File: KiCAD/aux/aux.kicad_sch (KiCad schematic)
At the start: 5 parts, among them J1 PMOD_male_2row, J2 Conn_01x12_Socket

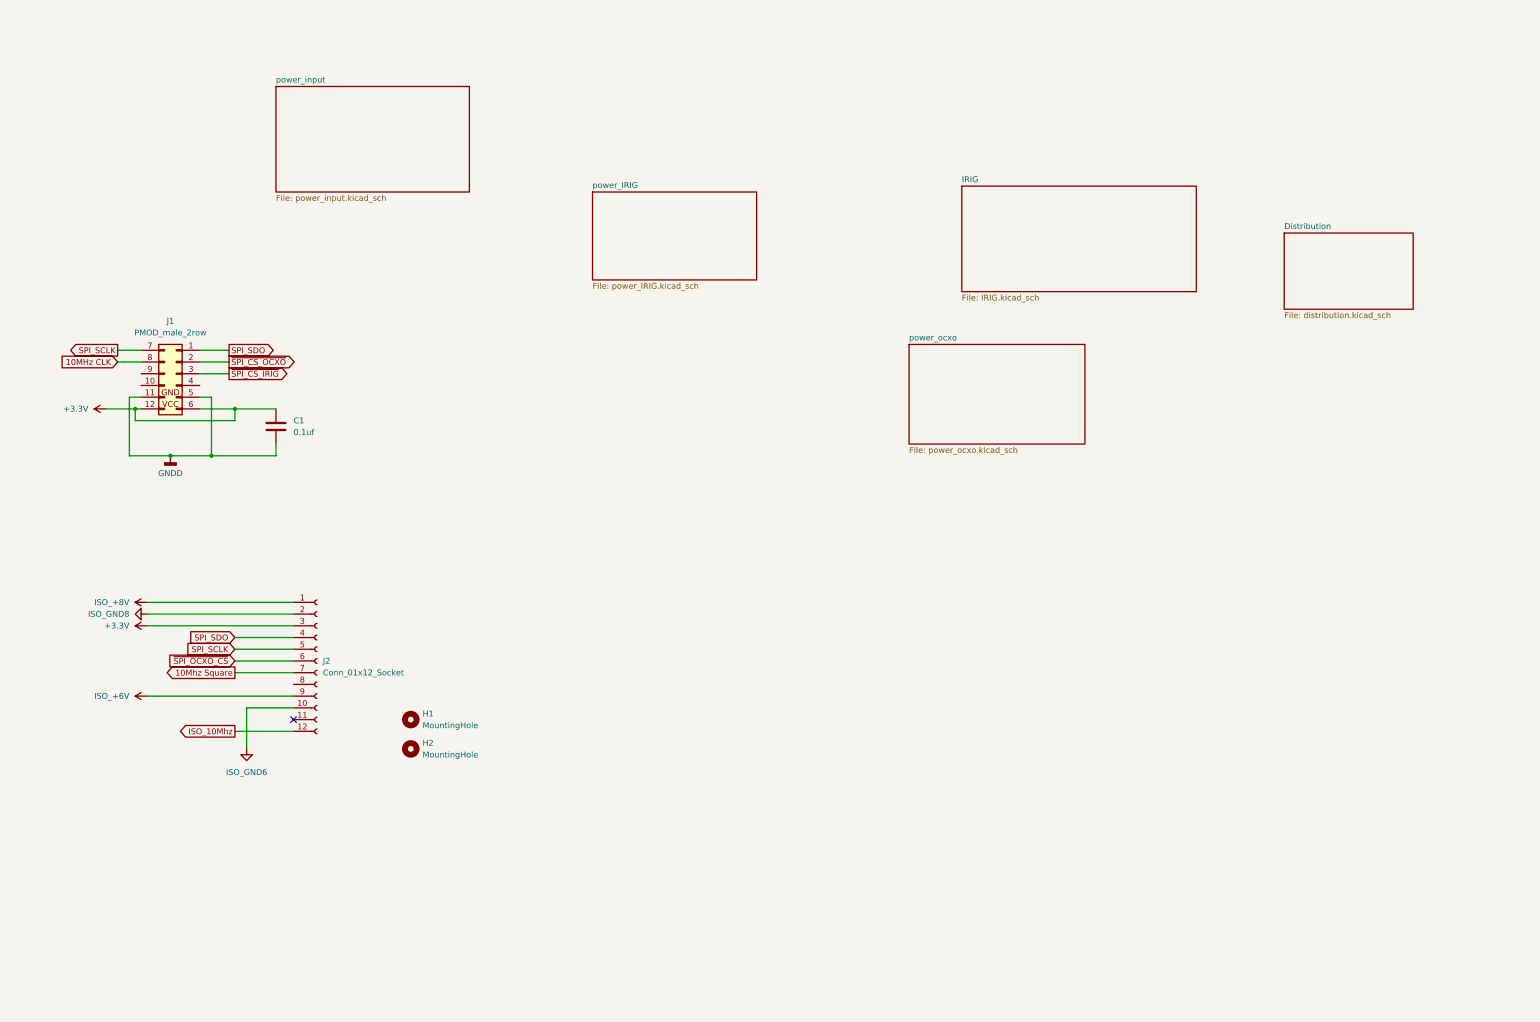
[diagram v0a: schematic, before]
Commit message: Reworked, now with IRIG option board complete
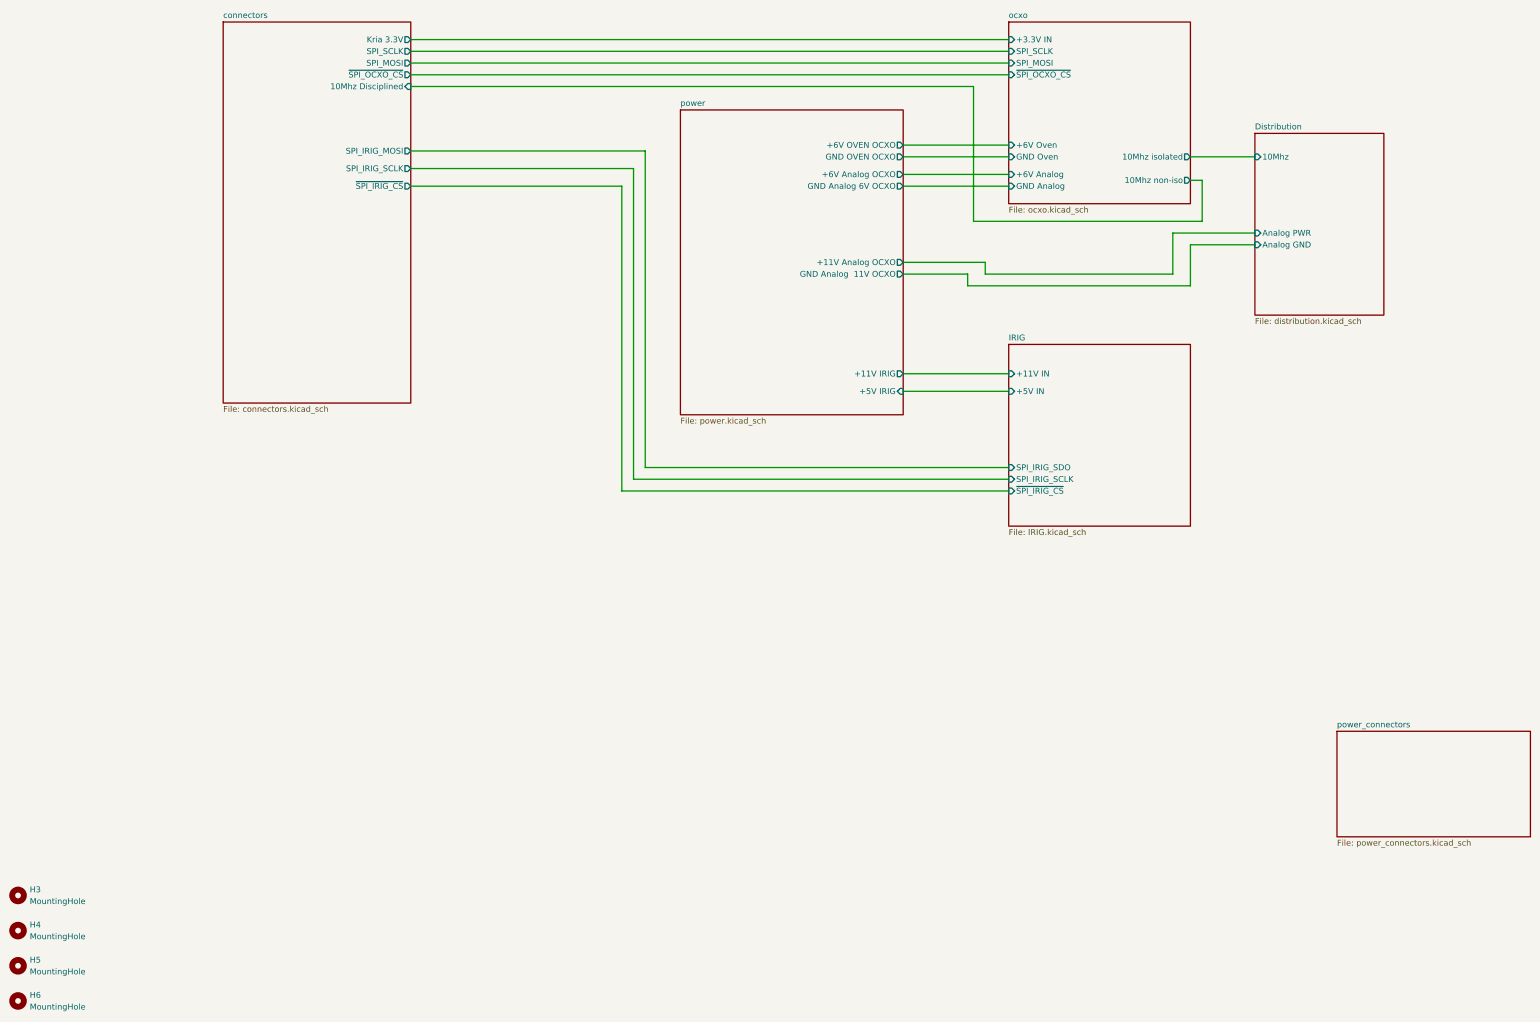
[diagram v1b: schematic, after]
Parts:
- removed C1: 0.1uf, Capacitor_SMD:C_1206_3216Metric_Pad1.33x1.80mm_HandSolder, symbol Device:C
- removed H1, H2: MountingHole, MountingHole:MountingHole_3.2mm_M3, symbol Mechanical:MountingHole
- removed J1: PMOD_male_2row, ! Scott:PMOD_male_12pin, symbol ! Scott:PMOD_male_2row
- removed J2: Conn_01x12_Socket, Connector_PinSocket_2.54mm:PinSocket_1x12_P2.54mm_Vertical, symbol Connector:Conn_01x12_Socket
- added H3, H4, H5, H6: MountingHole, MountingHole:MountingHole_3.2mm_M3, symbol Mechanical:MountingHole
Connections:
- no-connect marks 1 -> 0
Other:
- sheet power_input renamed power_connectors
- removed sheet power_IRIG
- removed sheet power_ocxo
- added sheet connectors (connectors.kicad_sch)
- added sheet ocxo (ocxo.kicad_sch)
- added sheet power (power.kicad_sch)
- sheet Distribution ports: added 10Mhz, Analog GND, Analog PWR; removed none
- sheet IRIG ports: added +11V IN, +5V IN, SPI_IRIG_SCLK, SPI_IRIG_SDO, ~{SPI_IRIG_CS}; removed none
- sheet power_connectors: file power_input.kicad_sch -> power_connectors.kicad_sch
